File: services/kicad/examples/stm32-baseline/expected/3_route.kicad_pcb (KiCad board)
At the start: 2 copper layers, 50.3 x 37.7 mm, 17 parts, among them J1 5V, U1 STM32F103C8T6, U2 AMS1117-3.3

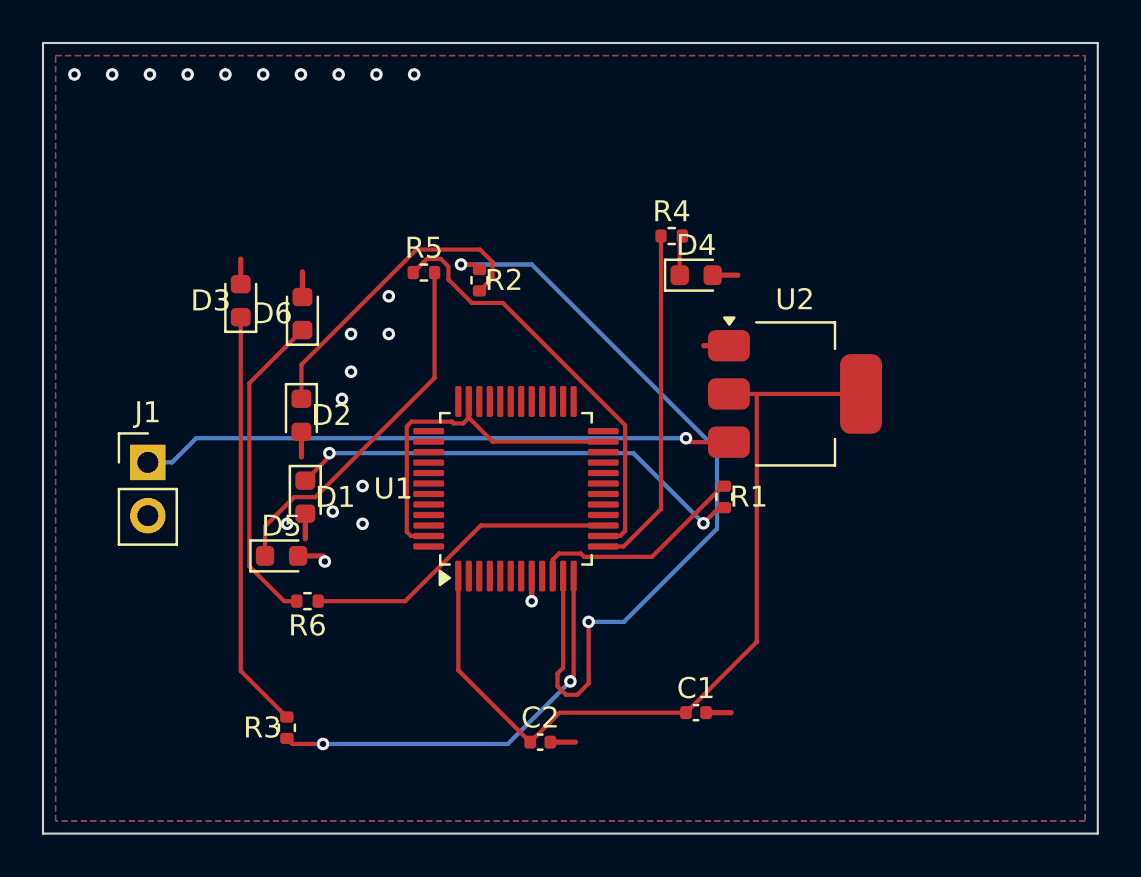
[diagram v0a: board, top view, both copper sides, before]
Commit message: test(examples): references stm32-*/esp32 -- 3_route.kicad_pcb et mesures-routage.json alignes sur les boards livres
Co-Authored-By: Claude Fable 5.1 <noreply@anthropic.com>
Claude-Session: https://claude.ai/code/session_01TnMqm4La2CxQHHB5K8aSSV
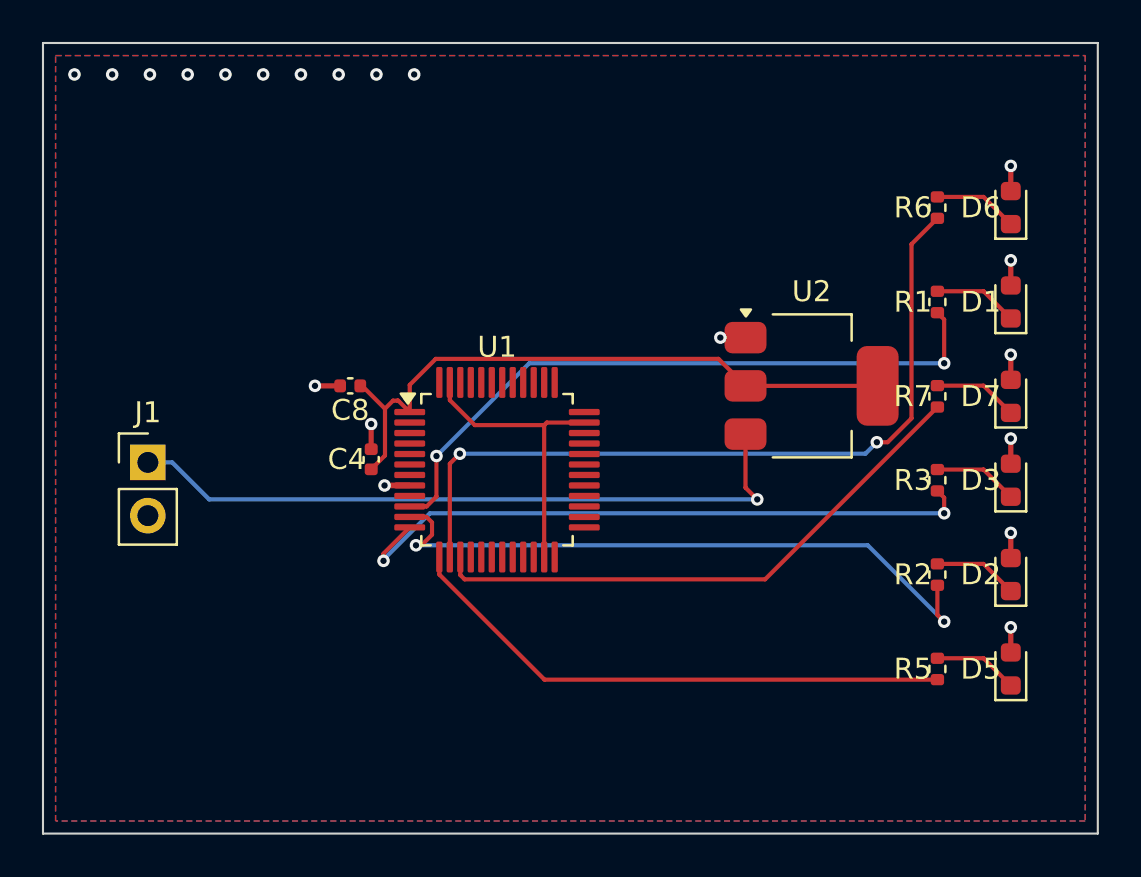
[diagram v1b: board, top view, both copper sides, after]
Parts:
- removed C1, C2: 100nF, C_0402_1005Metric
- removed D4: LED, LED_0603_1608Metric
- removed R4: 330, R_0402_1005Metric
- added C4: 100nF, C_0402_1005Metric, F.Cu at (139.0, 106.0)
- added C8: 100nF, C_0402_1005Metric, F.Cu at (138.0, 102.5)
- added D7: LED, LED_0603_1608Metric, F.Cu at (169.5, 103.0)
- added R7: 330, R_0402_1005Metric, F.Cu at (166.0, 103.0)
- moved D3 37.7 mm to (169.5, 107.0)
- moved R6 35.4 mm to (166.0, 94.0), turned to 90 degrees
- moved D5 35.2 mm to (169.5, 116.0), turned to 90 degrees
- moved D1 34.9 mm to (169.5, 98.5), turned to 90 degrees
- moved D2 34.7 mm to (169.5, 111.5), turned to 90 degrees
- moved D6 34.2 mm to (169.5, 94.0)
- moved R3 33.2 mm to (166.0, 107.0)
- moved R5 30.9 mm to (166.0, 116.0), turned to 90 degrees
- moved R2 26.0 mm to (166.0, 111.5), turned to 90 degrees
- moved R1 13.8 mm to (166.0, 98.5), turned to 90 degrees
- moved U1 1.28 mm to (145.0, 106.5), turned to 0 degrees
- moved U2 0.88 mm to (160.0, 102.5)
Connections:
- D5 pad 1: LED6 -> LED5
- D6 pad 1: LED7 -> LED6
- R5 pad 1: GPIO6 -> GPIO5
- R5 pad 2: LED6 -> LED5
- R6 pad 1: GPIO7 -> GPIO6
- R6 pad 2: LED7 -> LED6
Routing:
- net GPIO1: track 10.5 -> 32.0 mm, vias 0 -> 2
- net LED1: track 22.3 -> 4.04 mm, vias 2 -> 0
- net GPIO6: track 20.2 -> 37.4 mm, vias 0 -> 2
- net LED3: track 20.0 -> 4.04 mm
- net LED6: track 17.5 -> 4.04 mm
- net GPIO7: track 15.1 -> 27.1 mm
- net LED7: track 15.3 -> 4.04 mm
- net GPIO3: track 20.0 -> 31.0 mm
- net LED2: track 14.9 -> 4.04 mm
- net GPIO5: track 16.5 -> 26.7 mm
- net +3V3: track 40.2 -> 31.0 mm
- net GPIO2: track 38.8 -> 31.3 mm
- net VIN: track 28.3 -> 33.1 mm
- net Net-(U1-23): track 17.0 -> 14.1 mm
- net GND: track 12.0 -> 14.4 mm, vias 21 -> 20
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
